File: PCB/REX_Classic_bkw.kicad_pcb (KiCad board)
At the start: 2 copper layers, 38 x 16.6 mm, 12 parts, among them J1 Tandy_100_102_200_option_rom, J2 JTAG, J3 PRG, U1 XCR3064XL-VQ44, U2 29F800BB, U3 LP2980-3.3

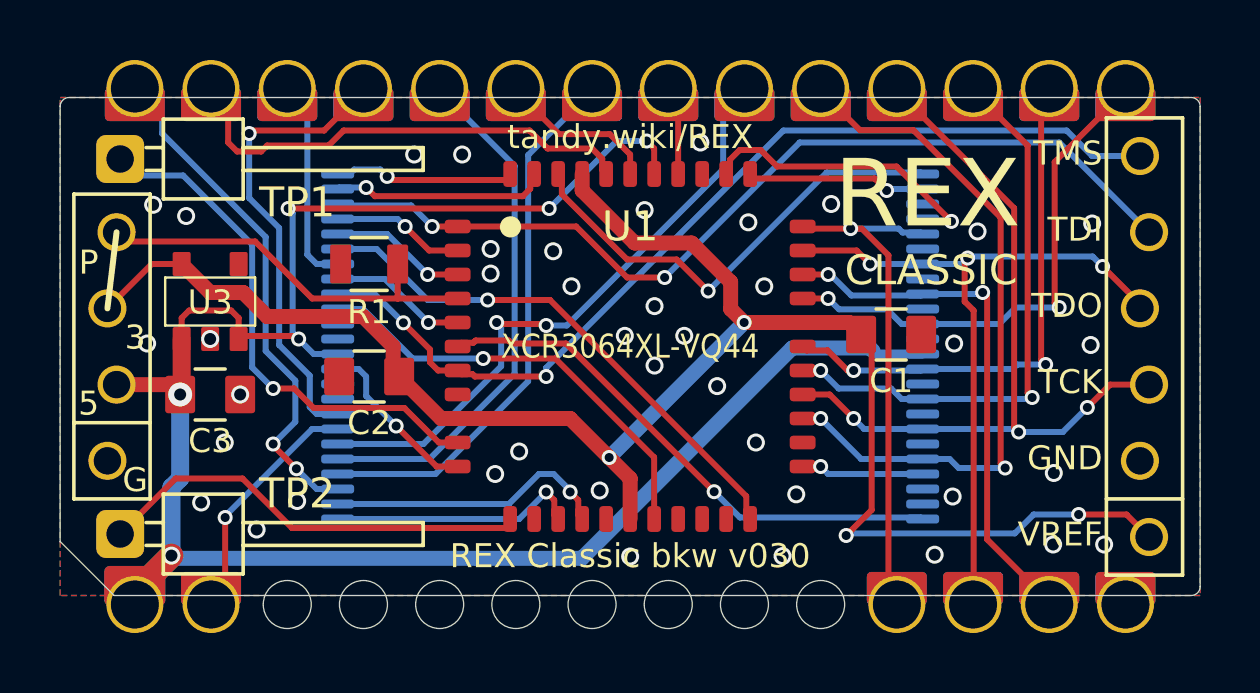
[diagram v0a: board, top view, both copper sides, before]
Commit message: 0805 footprints, minor trace adjustments
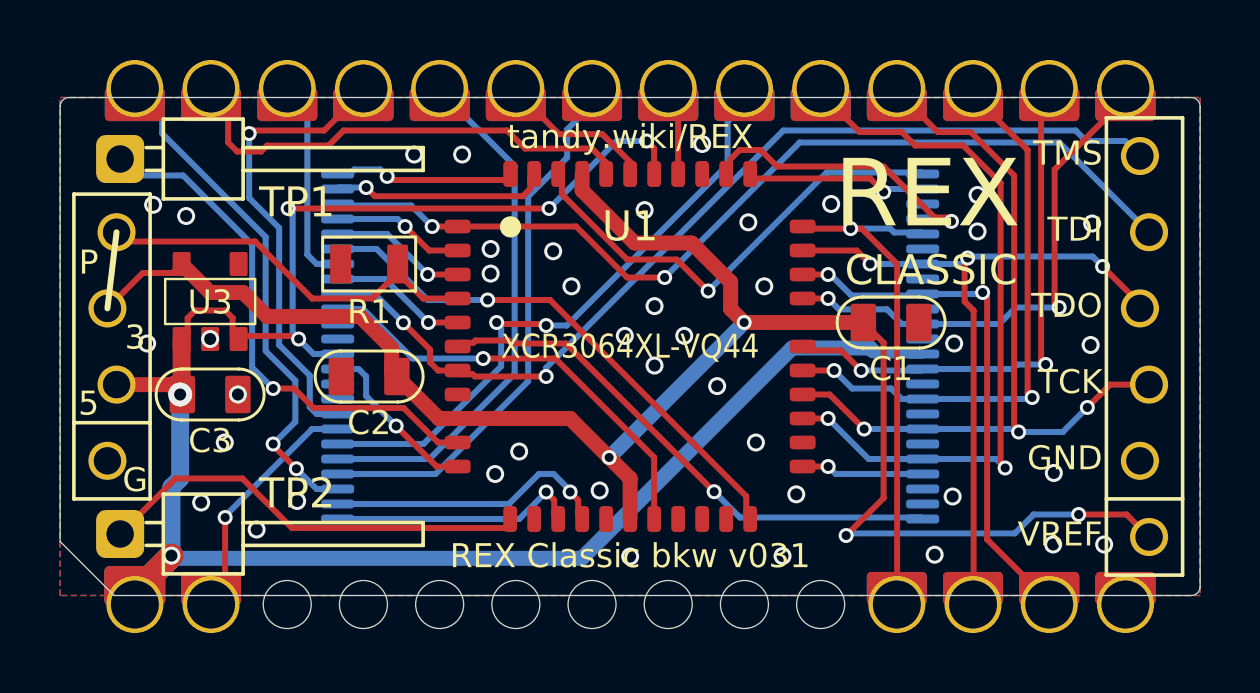
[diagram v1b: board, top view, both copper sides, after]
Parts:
- moved C1 0.40 mm to (145.9, 98.4)
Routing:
- net /D7: track 23.4 -> 24.1 mm
- net /D6/TCK: track 25.6 -> 26.2 mm
- net +3V3: track 59.4 -> 60.0 mm
- net GND: vias 41 -> 42
